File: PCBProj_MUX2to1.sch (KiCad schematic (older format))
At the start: 30 parts, among them J1 GS3, J2 GS3, J3 GS3, J4 GS3, J5 Socket_2mm, J6 Socket_2mm, U1 74HC00, U2 74HC00, X1 Conn_Coaxial, X2 Conn_Coaxial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

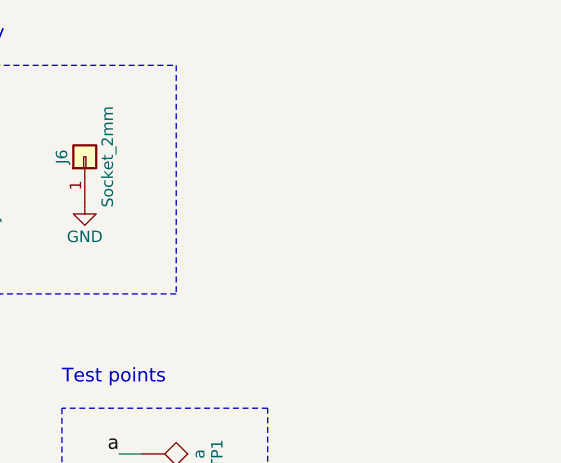
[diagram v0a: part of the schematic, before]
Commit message: Added holes for GND probes
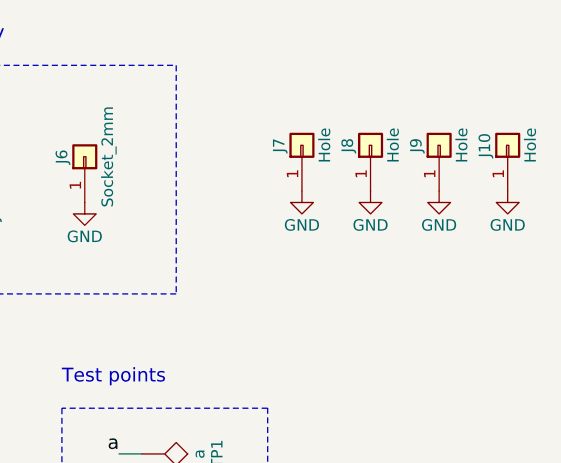
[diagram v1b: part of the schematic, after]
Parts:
- added J10, J7, J8, J9: Hole, Mounting_Holes:MountingHole_6mm_Pad, symbol Conn_01x01
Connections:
- net GND: now also J10.1 (Pin_1), J7.1 (Pin_1), J8.1 (Pin_1), J9.1 (Pin_1)
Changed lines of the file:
@@
 Wire Notes Line
 	6300 3600 6300 2300
+$Comp
+L Conn_01x01 J7
+U 1 1 5A50AE1F
+P 9250 1150
+F 0 "J7" H 9250 1250 50  0000 C CNN
+F 1 "Hole" H 9250 1050 50  0000 C CNN
+F 2 "Mounting_Holes:MountingHole_6mm_Pad" H 9250 1150 50  0001 C CNN
+F 3 "" H 9250 1150 50  0001 C CNN
+	1    9250 1150
+	0    -1   -1   0
+$EndComp
+$Comp
+L Conn_01x01 J8
+U 1 1 5A50AEB0
+P 9550 1150
+F 0 "J8" H 9550 1250 50  0000 C CNN
+F 1 "Hole" H 9550 1050 50  0000 C CNN
+F 2 "Mounting_Holes:MountingHole_6mm_Pad" H 9550 1150 50  0001 C CNN
+F 3 "" H 9550 1150 50  0001 C CNN
+	1    9550 1150
+	0    -1   -1   0
+$EndComp
+$Comp
+L Conn_01x01 J9
+U 1 1 5A50AF44
+P 9850 1150
+F 0 "J9" H 9850 1250 50  0000 C CNN
+F 1 "Hole" H 9850 1050 50  0000 C CNN
+F 2 "Mounting_Holes:MountingHole_6mm_Pad" H 9850 1150 50  0001 C CNN
+F 3 "" H 9850 1150 50  0001 C CNN
+	1    9850 1150
+	0    -1   -1   0
+$EndComp
+$Comp
+L Conn_01x01 J10
+U 1 1 5A50AFD9
+P 10150 1150
+F 0 "J10" H 10150 1250 50  0000 C CNN
+F 1 "Hole" H 10150 1050 50  0000 C CNN
+F 2 "Mounting_Holes:MountingHole_6mm_Pad" H 10150 1150 50  0001 C CNN
+F 3 "" H 10150 1150 50  0001 C CNN
+	1    10150 1150
+	0    -1   -1   0
+$EndComp
+$Comp
+L GND #PWR018
+U 1 1 5A50B06B
+P 9250 1350
+F 0 "#PWR018" H 9250 1100 50  0001 C CNN
+F 1 "GND" H 9250 1200 50  0000 C CNN
+F 2 "" H 9250 1350 50  0001 C CNN
+F 3 "" H 9250 1350 50  0001 C CNN
+	1    9250 1350
+	1    0    0    -1
+$EndComp
+$Comp
+L GND #PWR019
+U 1 1 5A50B0EE
+P 9550 1350
+F 0 "#PWR019" H 9550 1100 50  0001 C CNN
+F 1 "GND" H 9550 1200 50  0000 C CNN
+F 2 "" H 9550 1350 50  0001 C CNN
+F 3 "" H 9550 1350 50  0001 C CNN
+	1    9550 1350
+	1    0    0    -1
+$EndComp
+$Comp
+L GND #PWR020
+U 1 1 5A50B171
+P 9850 1350
+F 0 "#PWR020" H 9850 1100 50  0001 C CNN
+F 1 "GND" H 9850 1200 50  0000 C CNN
+F 2 "" H 9850 1350 50  0001 C CNN
+F 3 "" H 9850 1350 50  0001 C CNN
+	1    9850 1350
+	1    0    0    -1
+$EndComp
+$Comp
+L GND #PWR021
+U 1 1 5A50B1F4
+P 10150 1350
+F 0 "#PWR021" H 10150 1100 50  0001 C CNN
+F 1 "GND" H 10150 1200 50  0000 C CNN
+F 2 "" H 10150 1350 50  0001 C CNN
+F 3 "" H 10150 1350 50  0001 C CNN
+	1    10150 1350
+	1    0    0    -1
+$EndComp
 $EndSCHEMATC
